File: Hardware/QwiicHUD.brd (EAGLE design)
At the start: 25.4 x 25.4 mm, 27 parts, among them J4 WISECHIP_HUD_FPC

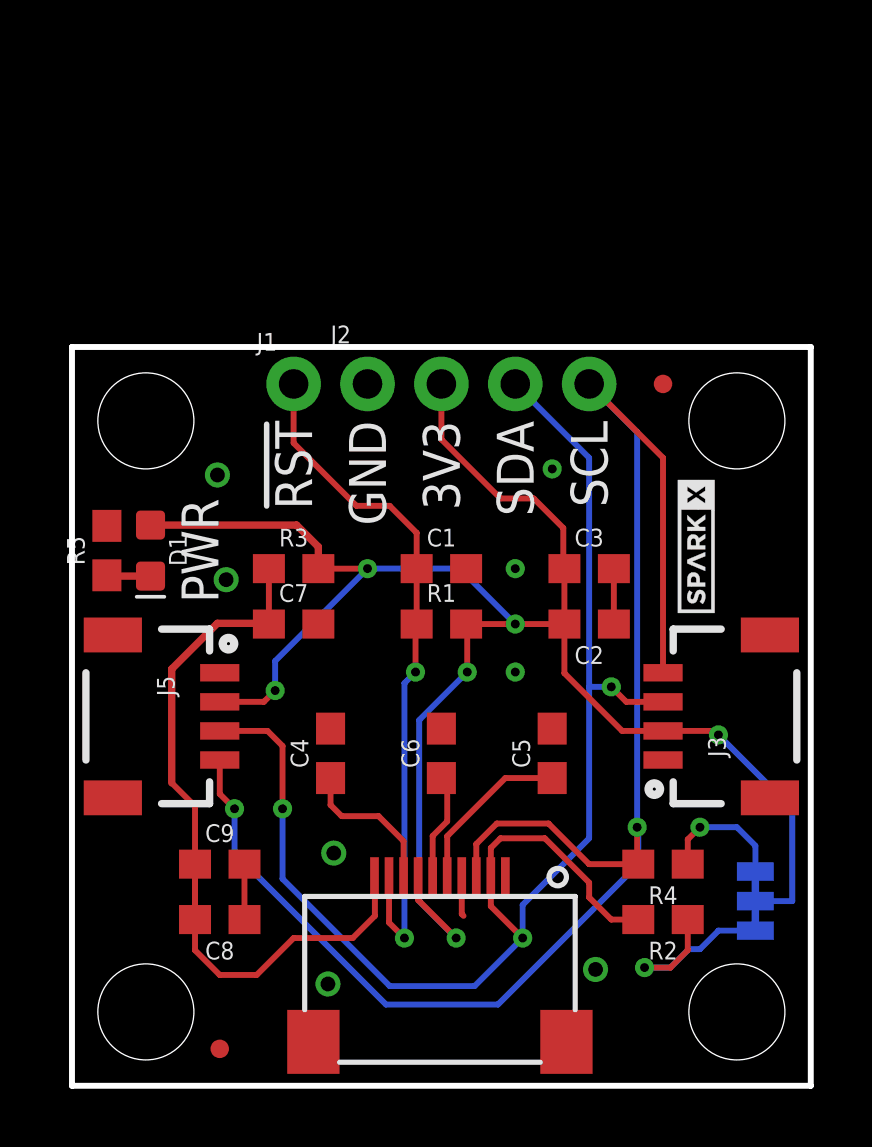
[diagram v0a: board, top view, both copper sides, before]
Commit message: x02
Added 12V boost circuit
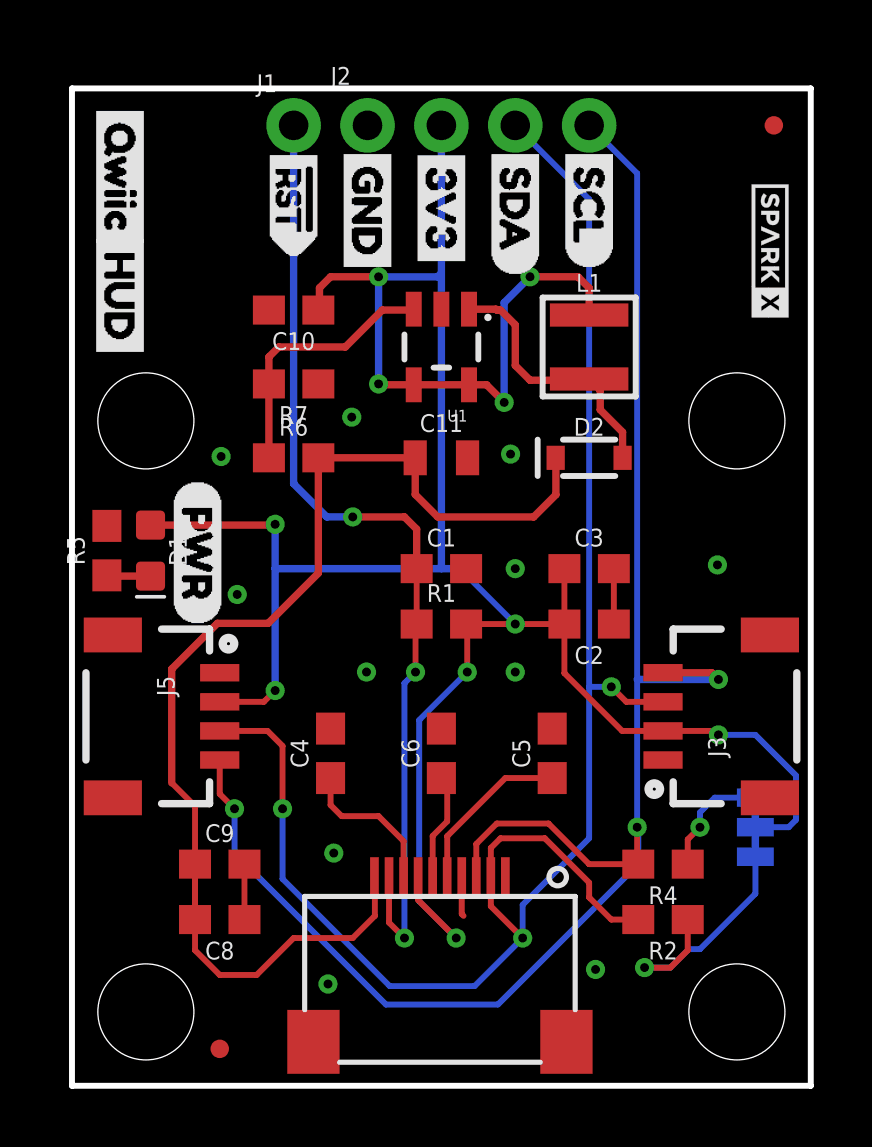
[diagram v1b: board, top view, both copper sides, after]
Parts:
- removed C7: 2.2uF, SparkFun-Capacitors:0603
- removed R3: 8.2k, SparkFun-Resistors:0603
- added C10: 1.0uF, SparkFun-Capacitors:0603
- added C11: 1.0uF/25V, SparkFun-Capacitors:0805
- added D2: 1A/23V/620mV, SparkFun-DiscreteSemi:SOD-323
- added L1: 10uH, 1.81_Greyscale_OLED_Breakout:INDUCTOR_3X3
- added R6: 47k, SparkFun-Resistors:0603
- added R7: 5.6k, SparkFun-Resistors:0603
- added U$1, U$14: (no value), Labels-0_04:#RST>
- added U$10, U$7: (no value), Labels-0_04:SDA
- added U$11, U$8: (no value), Labels-0_04:SCL
- added U$12, U$6: (no value), Labels-0_04:3V3
- added U$13, U$5: (no value), Labels-0_04:GND
- added U$16, U$18: (no value), buzzard_labels (1):QWIIC0
- added U$17, U$19: (no value), buzzard_labels (1):HUD1
- added U$20: (no value), Labels-0_04:(I_SUPER2_C)
- added U$9: (no value), Labels-0_04:(PWR)
- added U1: AP3012, 1.81_Greyscale_OLED_Breakout:SOT23-5
- R2, R4: value 4.7k -> 2.2k
- moved U$3 10.5 mm to (24.0, 28.7), turned to 270 degrees
- moved FD2 9.67 mm to (24.1, 33.0)
- moved J1 8.89 mm to (7.62, 33.0)
- moved J2 8.89 mm to (10.2, 33.0)
- moved JP1 2.54 mm to (23.5, 8.89)
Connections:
- net RST renamed !RST
- removed net VCC: C7.1, C8.2, C9.1, J4.1, R3.1
- new net 12V: C11.1, C8.2, C9.1, D2.C, J4.1, R6.2
- new net N$4: D2.A, L1.P$2, U1.1
- new net N$5: R6.1, R7.2, U1.3
- net 3.3V: now also C10.1, L1.P$1, U1.4, U1.5; no longer R3.2
- net GND: now also C10.2, C11.2, R7.1, U1.2; no longer C7.2
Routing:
- net 12V: track 0.00 -> 42.3 mm
- net VCC: track 26.6 -> 0.00 mm
- net 3.3V: track 66.8 -> 93.0 mm, vias 6 -> 10
- net !RST: track 24.0 -> 33.8 mm, vias 2 -> 3
- net N$4: track 0.00 -> 9.16 mm
- net N$5: track 0.00 -> 9.13 mm
- net SDA: track 51.4 -> 60.3 mm
- net SCL: track 58.5 -> 61.2 mm, vias 2 -> 3
- net N$1: track 7.12 -> 8.92 mm
- net GND: vias 8 -> 11
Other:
- board size 25.4 x 25.4 mm -> 25.4 x 34.3 mm
- board text removed: "!RST"
- board text removed: "3V3"
- board text removed: "GND"
- board text removed: "I2C PU"
- board text removed: "PWR"
- board text removed: "Qwiic HUD"
- board text removed: "RST"
- board text removed: "SCL"
- board text removed: "SDA"
